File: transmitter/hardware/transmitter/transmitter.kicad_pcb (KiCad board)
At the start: 2 copper layers, 56 x 47 mm, 40 parts, among them J1 SOIL, J2 SOIL, J3 USB_UART, J4 PWR, J5 SOIL, J6 SOIL, J7 SOIL, J8 SOIL, Q1 Si2305CDS, Q2 BSS138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

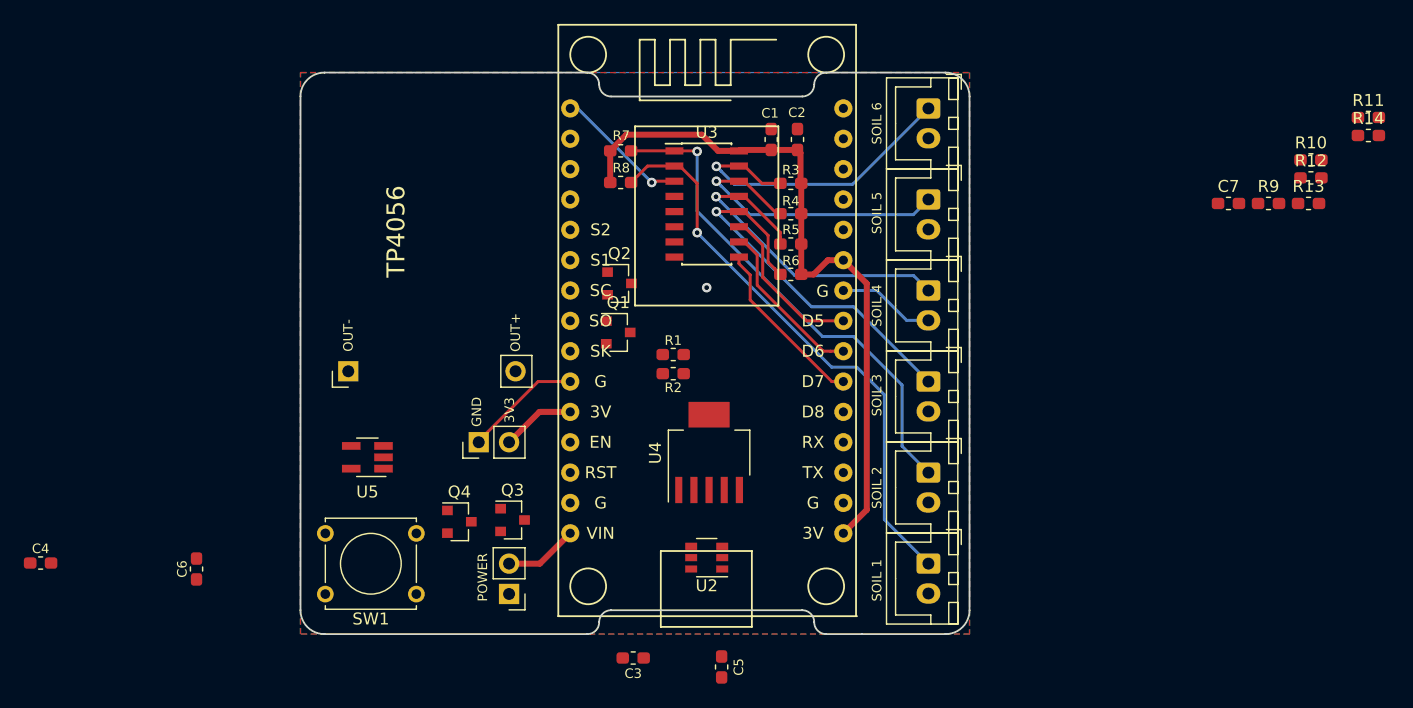
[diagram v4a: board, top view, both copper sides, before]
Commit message: Wired the low voltage cutoff
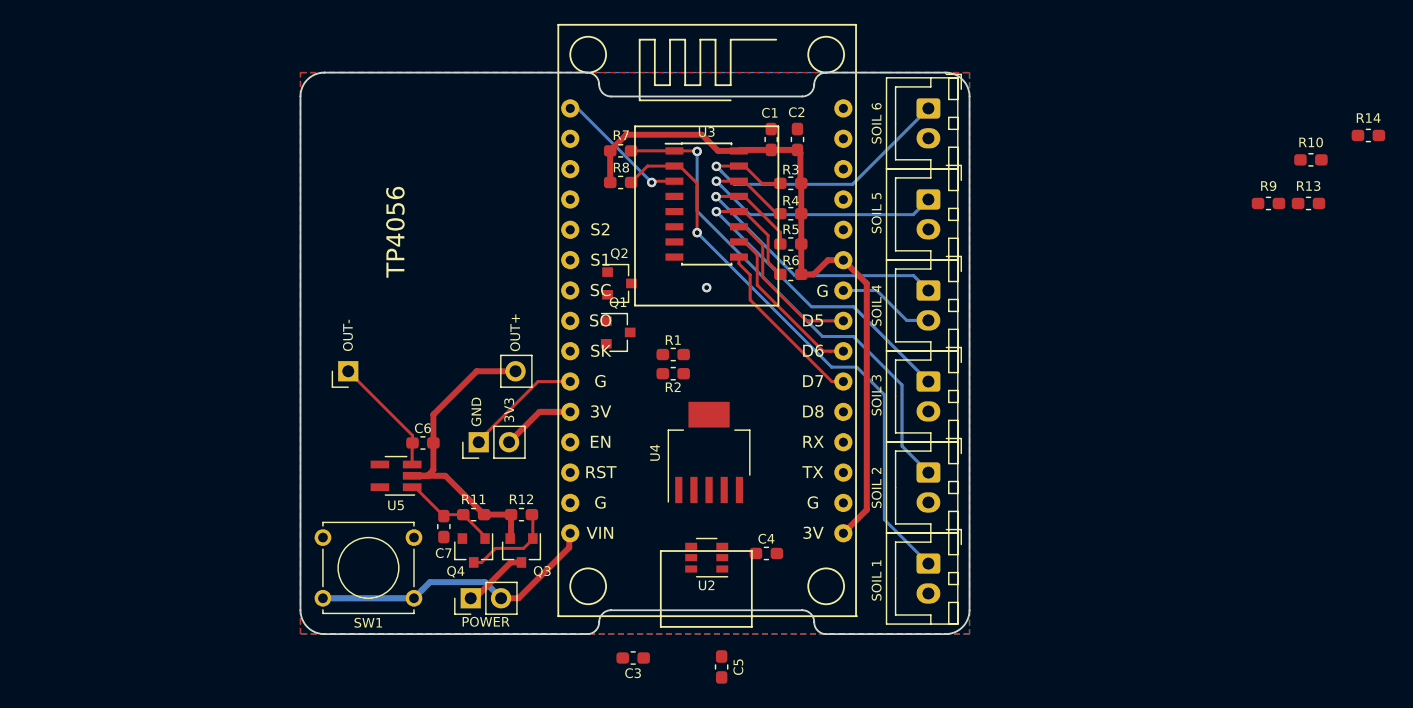
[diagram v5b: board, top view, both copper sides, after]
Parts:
- moved R11 81.9 mm to (129.1, 101.9), turned to 180 degrees
- moved R12 71.8 mm to (133.1, 101.9)
- moved C7 71.0 mm to (126.6, 102.9), turned to 270 degrees
- moved C4 60.8 mm to (153.6, 105.2)
- moved C6 21.7 mm to (124.9, 95.9), turned to 180 degrees
- moved SW2 3.23 mm to (128.9, 108.9), turned to 90 degrees
- moved U5 2.86 mm to (122.6, 98.7)
- moved Q4 2.68 mm to (129.1, 104.9), turned to 270 degrees
- moved Q3 2.66 mm to (133.1, 104.9), turned to 270 degrees
- moved SW1 0.40 mm to (124.1, 108.9)
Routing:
- net /OUT+: track 0.00 -> 26.6 mm
- net /VBAT: track 6.38 -> 24.9 mm
- net GND: track 17.4 -> 27.4 mm
- net Net-(C7-Pad1): track 0.00 -> 8.09 mm
- net Net-(Q3-Pad1): track 0.00 -> 7.84 mm
- net Net-(Q3-Pad3): track 0.00 -> 5.49 mm
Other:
- rule pad_to_mask_clearance: 0.051 -> 0

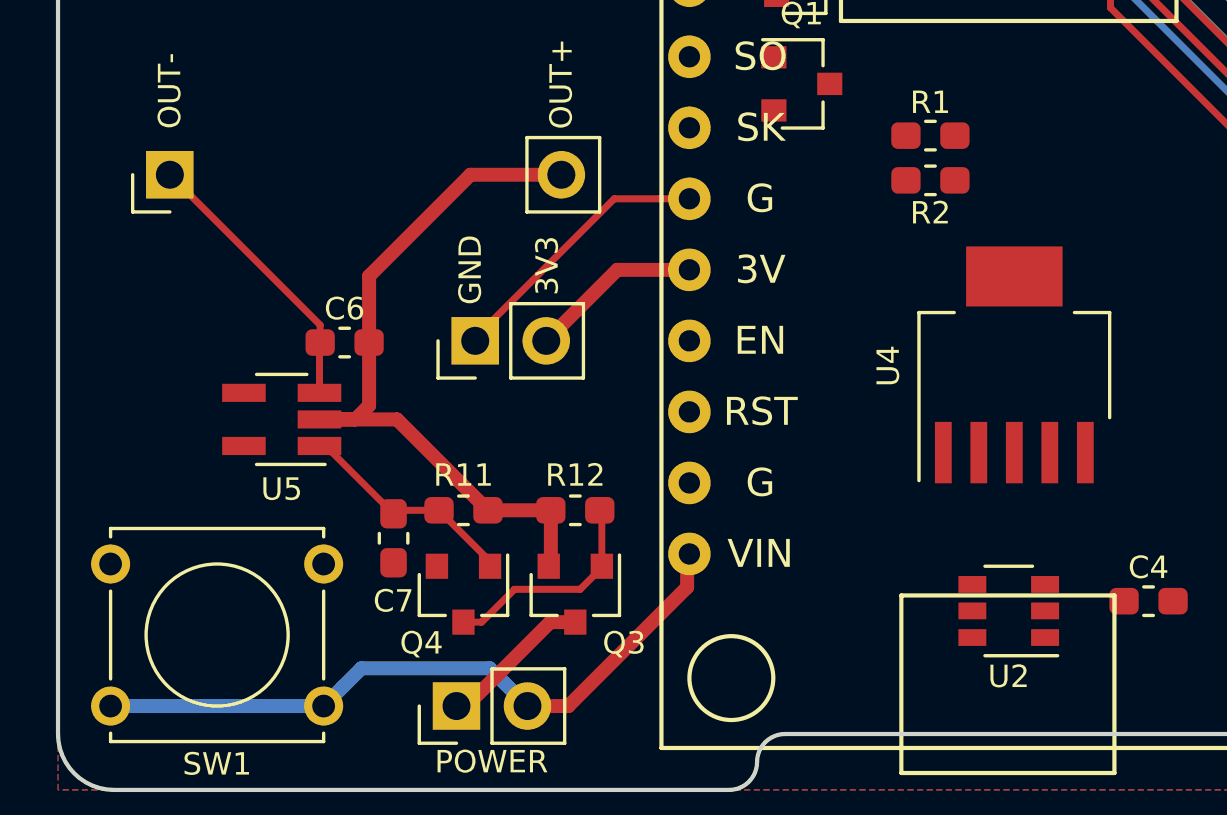
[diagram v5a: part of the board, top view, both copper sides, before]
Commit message: Power led
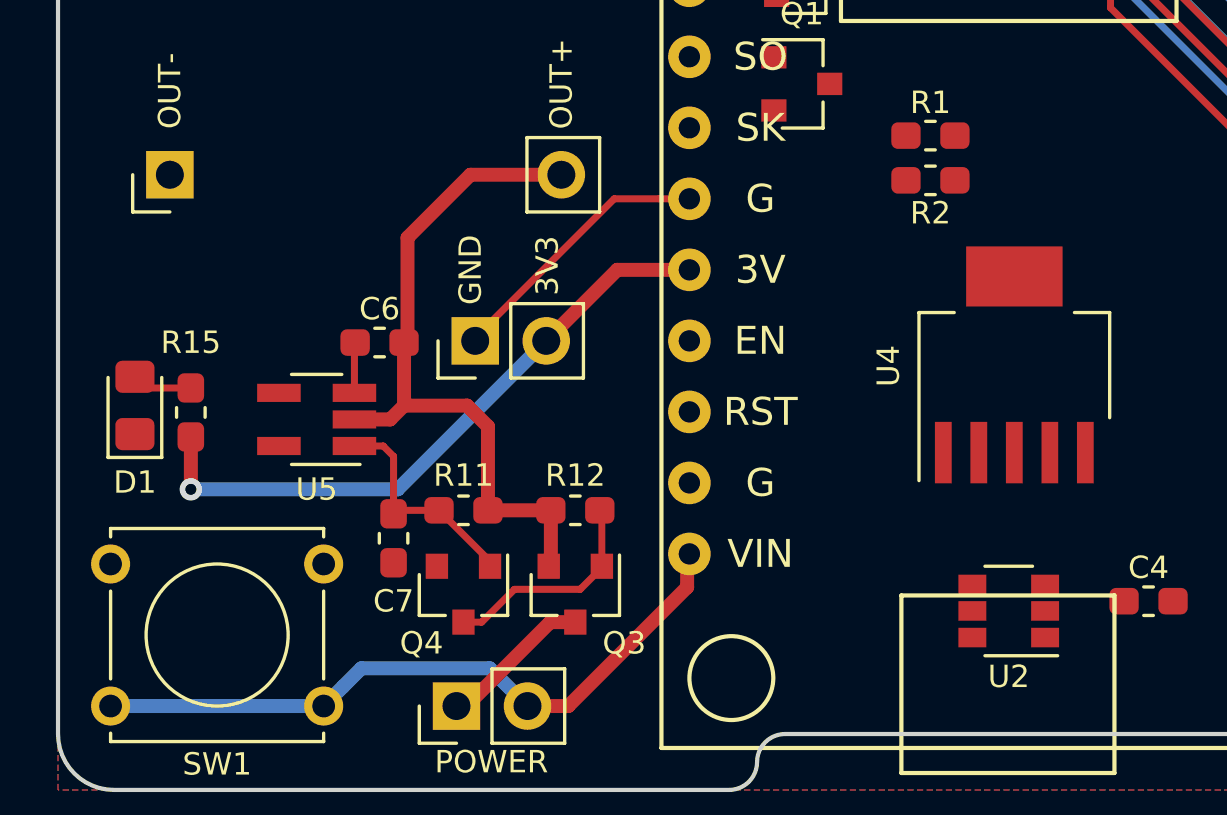
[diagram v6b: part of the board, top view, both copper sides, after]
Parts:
- added D1: LED, LED_SMD:LED_0805_2012Metric_Pad1.15x1.40mm_HandSolder, F.Cu at (117.4, 98.2)
- added R15: 1K, Resistor_SMD:R_0603_1608Metric_Pad1.05x0.95mm_HandSolder, F.Cu at (119.4, 98.4)
- U2: footprint tpl511x:SOT-6-DDC -> Package_TO_SOT_SMD:SuperSOT-6
- moved C6 1.25 mm to (126.1, 95.9)
- moved U5 1.25 mm to (123.9, 98.7)
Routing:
- net 3V3: track 64.7 -> 81.5 mm, vias 0 -> 1
- net GND: track 27.4 -> 19.2 mm
- net Net-(D1-Pad2): track 0.00 -> 2.17 mm
- net /OUT+: track 26.6 -> 25.1 mm

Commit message: Wired
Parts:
- moved R10 59.4 mm to (143.9, 93.9)
- moved R14 59.0 mm to (152.4, 98.7), turned to 180 degrees
- moved R13 53.1 mm to (152.4, 101.3)
- moved R9 50.4 mm to (148.6, 93.9), turned to 180 degrees
- moved Q2 8.73 mm to (143.9, 90.9), turned to 90 degrees
- moved C5 8.70 mm to (145.1, 107.4), turned to 0 degrees
- moved Q1 8.53 mm to (148.6, 90.9), turned to 90 degrees
- moved C3 8.36 mm to (141.1, 105.7), turned to 270 degrees
- moved U4 5.89 mm to (145.5, 101.6)
- moved R2 3.96 mm to (143.9, 86.7)
- moved C4 3.86 mm to (156.8, 107.3), turned to 0 degrees
- moved U2 3.83 mm to (152.4, 106.3)
- moved R1 3.36 mm to (148.6, 86.7), turned to 180 degrees
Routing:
- net 3V3: track 81.5 -> 132.3 mm
- net DONE: track 0.00 -> 50.2 mm, vias 0 -> 2
- net /VBAT: track 24.9 -> 68.8 mm, vias 0 -> 1
- net Net-(R13-Pad2): track 0.00 -> 42.9 mm, vias 0 -> 1
- net GND: track 19.2 -> 42.8 mm
- net BATT_SENSE: track 0.00 -> 15.3 mm
- net Net-(Q1-Pad1): track 0.00 -> 6.69 mm
- net Net-(U2-Pad5): track 0.00 -> 4.33 mm
- net Net-(Q1-Pad3): track 0.00 -> 3.99 mm
- net Net-(R13-Pad1): track 0.00 -> 2.60 mm
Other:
- outline, holes or cut-outs redrawn
- board text added: "TIME"
- board text added: "https://github.com/theapi/ esp8266wsn Rev 2.0.0"
- board text removed: "https://github.com/theapi/ esp8266wsn v 1.0.0"

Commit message: Logos
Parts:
- added REF**: TheApiLogo, theapi:TheApiLogo, B.Cu at (126.0, 78.2)
- added REF**: TheApiLogoTiny, theapi:TheApiLogoTiny, F.Cu at (126.2, 107.2)
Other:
- board text added: "https://github.com/theapi/esp8266wsn Jan 2020 Rev 2.0.0"
- board text removed: "https://github.com/theapi/ esp8266wsn Rev 2.0.0"
